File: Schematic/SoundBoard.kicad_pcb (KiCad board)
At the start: 4 copper layers, 50 x 50 mm, 50 parts, among them J1 USB_B_Micro, J2 Conn_ARM_JTAG_SWD_10, SW1 SW_Push, SW2 SW_Push, U1 AMS1117-3.3, U2 STM32F405RGTx, U3 MCP4021-xxxxSN, U4 LM4562, U5 W25Q128JVS, Y1 25Mhz

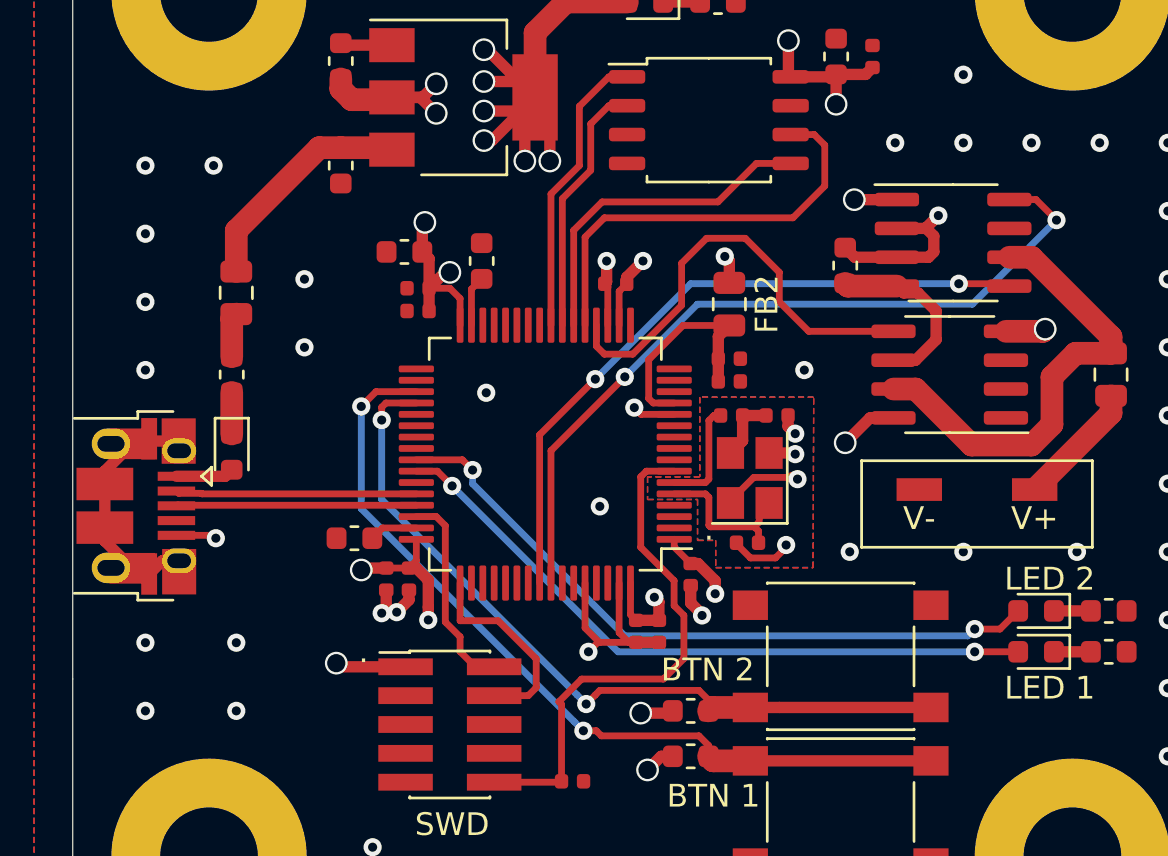
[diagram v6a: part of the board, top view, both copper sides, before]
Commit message: Modify manufacturing output per JLC
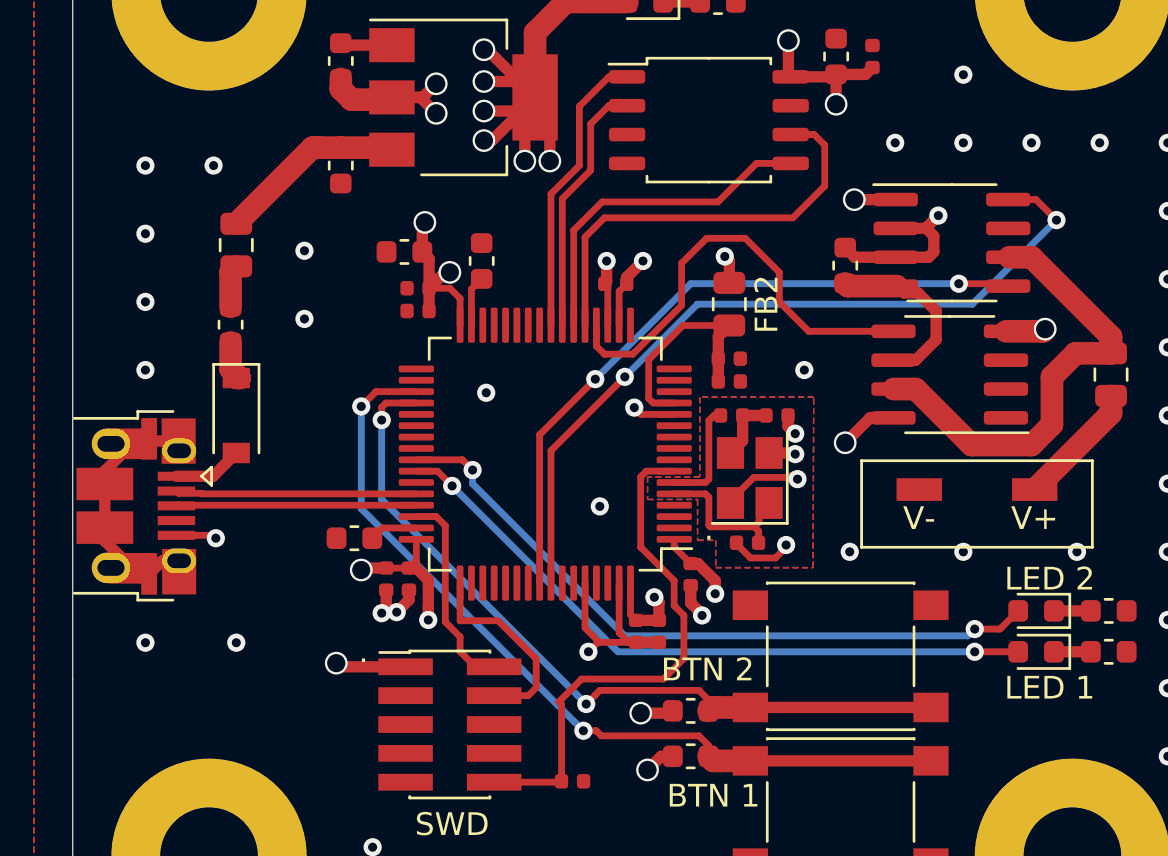
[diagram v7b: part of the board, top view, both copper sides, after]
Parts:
- D1: footprint Diode_SMD:D_0603_1608Metric -> Diode_SMD:D_SOD-123
- moved F1 2.20 mm to (66.8, 112.0)
- moved FB1 2.10 mm to (67.0, 108.5)
- moved D1 1.61 mm to (67.0, 116.0)
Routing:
- net Net-(C1-Pad1): track 10.2 -> 8.27 mm
- net VDD: track 2.55 -> 3.06 mm
- net GND: vias 65 -> 63
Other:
- board text added: "JLCJLCJLCJLC"
- board text removed: "JLCJLCJLC"
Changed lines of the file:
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@@
   )
   (setup
-    (last_trace_width 0.5)
+    (last_trace_width 1)
     (user_trace_width 0.3)
     (user_trace_width 0.4)
@@
     (add_net VDD)
   )
+  (module Diode_SMD:D_SOD-123 (layer F.Cu)
+    (at 67 116 270)
+    (descr SOD-123)
+    (tags SOD-123)
+    (attr smd)
+    (fp_text reference D1 (at 0 -2 90) (layer F.Fab)
+      (effects (font (size 1 1) (thickness 0.15)))
+    )
+    (fp_text value D_Schottky (at -0.25 -3 90) (layer F.Fab)
+      (effects (font (size 1 1) (thickness 0.15)))
+    )
+    (fp_line (start -2.25 -1) (end 1.65 -1) (layer F.SilkS) (width 0.12))
+    (fp_line (start -2.25 1) (end 1.65 1) (layer F.SilkS) (width 0.12))
+    (fp_line (start -2.35 -1.15) (end -2.35 1.15) (layer F.CrtYd) (width 0.05))
+    (fp_line (start 2.35 1.15) (end -2.35 1.15) (layer F.CrtYd) (width 0.05))
+    (fp_line (start 2.35 -1.15) (end 2.35 1.15) (layer F.CrtYd) (width 0.05))
+    (fp_line (start -2.35 -1.15) (end 2.35 -1.15) (layer F.CrtYd) (width 0.05))
+    (fp_line (start -1.4 -0.9) (end 1.4 -0.9) (layer F.Fab) (width 0.1))
+    (fp_line (start 1.4 -0.9) (end 1.4 0.9) (layer F.Fab) (width 0.1))
+    (fp_line (start 1.4 0.9) (end -1.4 0.9) (layer F.Fab) (width 0.1))
+    (fp_line (start -1.4 0.9) (end -1.4 -0.9) (layer F.Fab) (width 0.1))
+    (fp_line (start -0.75 0) (end -0.35 0) (layer F.Fab) (width 0.1))
+    (fp_line (start -0.35 0) (end -0.35 -0.55) (layer F.Fab) (width 0.1))
+    (fp_line (start -0.35 0) (end -0.35 0.55) (layer F.Fab) (width 0.1))
+    (fp_line (start -0.35 0) (end 0.25 -0.4) (layer F.Fab) (width 0.1))
+    (fp_line (start 0.25 -0.4) (end 0.25 0.4) (layer F.Fab) (width 0.1))
+    (fp_line (start 0.25 0.4) (end -0.35 0) (layer F.Fab) (width 0.1))
+    (fp_line (start 0.25 0) (end 0.75 0) (layer F.Fab) (width 0.1))
+    (fp_line (start -2.25 -1) (end -2.25 1) (layer F.SilkS) (width 0.12))
+    (fp_text user %R (at 0 -2 90) (layer F.Fab)
+      (effects (font (size 1 1) (thickness 0.15)))
+    )
+    (pad 2 smd rect (at 1.65 0 270) (size 0.9 1.2) (layers F.Cu F.Paste F.Mask)
+      (net 17 VDD))
+    (pad 1 smd rect (at -1.65 0 270) (size 0.9 1.2) (layers F.Cu F.Paste F.Mask)
+      (net 3 "Net-(D1-Pad1)"))
+    (model ${KISYS3DMOD}/Diode_SMD.3dshapes/D_SOD-123.wrl
+      (at (xyz 0 0 0))
+      (scale (xyz 1 1 1))
+      (rotate (xyz 0 0 0))
+    )
+  )
   (module Package_SO:SOIC-8_3.9x4.9mm_P1.27mm (layer F.Cu)
     (at 98.4 114.2 180)
@@
   )
   (module Inductor_SMD:L_0805_2012Metric (layer F.Cu)
-    (at 67 110.6 270)
+    (at 67 108.5 270)
     (descr "Inductor SMD 0805 (2012 Metric), square (rectangular) end terminal, IPC_7351 nominal, (Body size source: https://docs.google.com/spreadsheets/d/1BsfQQcO9C6DZCsRaXUlFlo91Tg2WpOkGARC1WS5S8t0/edit?usp=sharing), generated with kicad-footprint-generator")
     (tags inductor)
@@
     )
   )
-  (module Diode_SMD:D_0603_1608Metric (layer F.Cu)
-    (at 66.8 117.6 270)
-    (descr "Diode SMD 0603 (1608 Metric), square (rectangular) end terminal, IPC_7351 nominal, (Body size source: http://www.tortai-tech.com/upload/download/2011102023233369053.pdf), generated with kicad-footprint-generator")
-    (tags diode)
-    (attr smd)
-    (fp_text reference D1 (at 0 -1.43 90) (layer F.Fab)
-      (effects (font (size 1 1) (thickness 0.15)))
-    )
-    (fp_text value D_Schottky (at 0.2 -5 180) (layer F.Fab)
-      (effects (font (size 1 1) (thickness 0.15)))
-    )
-    (fp_line (start 0.8 -0.4) (end -0.5 -0.4) (layer F.Fab) (width 0.1))
-    (fp_line (start -0.5 -0.4) (end -0.8 -0.1) (layer F.Fab) (width 0.1))
-    (fp_line (start -0.8 -0.1) (end -0.8 0.4) (layer F.Fab) (width 0.1))
-    (fp_line (start -0.8 0.4) (end 0.8 0.4) (layer F.Fab) (width 0.1))
-    (fp_line (start 0.8 0.4) (end 0.8 -0.4) (layer F.Fab) (width 0.1))
-    (fp_line (start 0.8 -0.735) (end -1.485 -0.735) (layer F.SilkS) (width 0.12))
-    (fp_line (start -1.485 -0.735) (end -1.485 0.735) (layer F.SilkS) (width 0.12))
-    (fp_line (start -1.485 0.735) (end 0.8 0.735) (layer F.SilkS) (width 0.12))
-    (fp_line (start -1.48 0.73) (end -1.48 -0.73) (layer F.CrtYd) (width 0.05))
-    (fp_line (start -1.48 -0.73) (end 1.48 -0.73) (layer F.CrtYd) (width 0.05))
-    (fp_line (start 1.48 -0.73) (end 1.48 0.73) (layer F.CrtYd) (width 0.05))
-    (fp_line (start 1.48 0.73) (end -1.48 0.73) (layer F.CrtYd) (width 0.05))
-    (fp_text user %R (at 0 0 90) (layer F.Fab)
-      (effects (font (size 0.4 0.4) (thickness 0.06)))
-    )
-    (pad 1 smd roundrect (at -0.7875 0 270) (size 0.875 0.95) (layers F.Cu F.Paste F.Mask) (roundrect_rratio 0.25)
-      (net 3 "Net-(D1-Pad1)"))
-    (pad 2 smd roundrect (at 0.7875 0 270) (size 0.875 0.95) (layers F.Cu F.Paste F.Mask) (roundrect_rratio 0.25)
-      (net 17 VDD))
-    (model ${KISYS3DMOD}/Diode_SMD.3dshapes/D_0603_1608Metric.wrl
-      (at (xyz 0 0 0))
-      (scale (xyz 1 1 1))
-      (rotate (xyz 0 0 0))
-    )
-  )
   (module LED_SMD:LED_0603_1608Metric (layer F.Cu)
     (at 85 97.8 180)
@@
   )
   (module Fuse:Fuse_0603_1608Metric (layer F.Cu)
-    (at 66.8 114.2 270)
+    (at 66.75 112 270)
     (descr "Fuse SMD 0603 (1608 Metric), square (rectangular) end terminal, IPC_7351 nominal, (Body size source: http://www.tortai-tech.com/upload/download/2011102023233369053.pdf), generated with kicad-footprint-generator")
     (tags resistor)
@@
   )
   (module Package_SO:SOIC-8_3.9x4.9mm_P1.27mm (layer F.Cu)
-    (at 98.55 108.4)
+    (at 98.5 108.4)
     (descr "SOIC, 8 Pin (JEDEC MS-012AA, https://www.analog.com/media/en/package-pcb-resources/package/pkg_pdf/soic_narrow-r/r_8.pdf), generated with kicad-footprint-generator ipc_gullwing_generator.py")
     (tags "SOIC SO")
@@
     (effects (font (size 1 1) (thickness 0.15)) (justify mirror))
   )
-  (gr_text JLCJLCJLC (at 65.4 128.8) (layer B.SilkS)
+  (gr_text "JLCJLCJLCJLC\n" (at 68.5 129.25) (layer B.SilkS)
     (effects (font (size 1 1) (thickness 0.15)) (justify mirror))
   )
@@
   (via (at 74.061026 124.655978) (size 0.8) (drill 0.4) (layers F.Cu B.Cu) (net 1))
   (segment (start 74.6 124.117004) (end 74.061026 124.655978) (width 0.5) (layer F.Cu) (net 1))
-  (via (at 70 110) (size 0.8) (drill 0.4) (layers F.Cu B.Cu) (net 1))
-  (via (at 70 113) (size 0.8) (drill 0.4) (layers F.Cu B.Cu) (net 1))
+  (via (at 70 108.75) (size 0.8) (drill 0.4) (layers F.Cu B.Cu) (net 1))
+  (via (at 70 111.75) (size 0.8) (drill 0.4) (layers F.Cu B.Cu) (net 1))
   (via (at 78 115) (size 0.8) (drill 0.4) (layers F.Cu B.Cu) (net 1))
   (via (at 63 105) (size 0.8) (drill 0.4) (layers F.Cu B.Cu) (net 1))
@@
   (via (at 63 111) (size 0.8) (drill 0.4) (layers F.Cu B.Cu) (net 1))
   (via (at 63 126) (size 0.8) (drill 0.4) (layers F.Cu B.Cu) (net 1))
-  (via (at 63 129) (size 0.8) (drill 0.4) (layers F.Cu B.Cu) (net 1))
-  (via (at 67 129) (size 0.8) (drill 0.4) (layers F.Cu B.Cu) (net 1))
   (via (at 67 126) (size 0.8) (drill 0.4) (layers F.Cu B.Cu) (net 1))
   (via (at 73 135) (size 0.8) (drill 0.4) (layers F.Cu B.Cu) (net 1))
@@
   (segment (start 105.5 115.9) (end 105.5 115.1375) (width 1) (layer F.Cu) (net 2))
   (segment (start 102.14 119.26) (end 105.5 115.9) (width 1) (layer F.Cu) (net 2))
-  (segment (start 66.8 116.8125) (end 66.8 114.9875) (width 1) (layer F.Cu) (net 3))
+  (segment (start 67 114.35) (end 67.15 114.35) (width 1) (layer F.Cu) (net 3))
+  (segment (start 66.75 113.95) (end 66.75 112.7875) (width 1) (layer F.Cu) (net 3))
+  (segment (start 67.15 114.35) (end 66.75 113.95) (width 1) (layer F.Cu) (net 3))
   (segment (start 87.4125 97.8) (end 85.7875 97.8) (width 0.5) (layer F.Cu) (net 4))
   (segment (start 102.9875 126.4) (end 104.6125 126.4) (width 0.5) (layer F.Cu) (net 5))
@@
   (segment (start 73.7625 104.2125) (end 73.85 104.3) (width 1) (layer F.Cu) (net 9))
   (segment (start 71.6 104.2125) (end 73.7625 104.2125) (width 1) (layer F.Cu) (net 9))
-  (segment (start 67 107.8625) (end 70.65 104.2125) (width 1) (layer F.Cu) (net 9))
-  (segment (start 67 109.6625) (end 67 107.8625) (width 1) (layer F.Cu) (net 9))
+  (segment (start 70.35 104.2125) (end 70.65 104.2125) (width 1) (layer F.Cu) (net 9))
+  (segment (start 67 107.5625) (end 70.35 104.2125) (width 1) (layer F.Cu) (net 9))
   (segment (start 90.085 120.215) (end 90.45 119.85) (width 0.3) (layer F.Cu) (net 10))
   (segment (start 87.799999 119.599999) (end 87.799999 120.830001) (width 0.3) (layer F.Cu) (net 10))
@@
   (segment (start 102 109.035) (end 105.5 112.535) (width 1) (layer F.Cu) (net 16))
   (segment (start 101.025 109.035) (end 102 109.035) (width 1) (layer F.Cu) (net 16))
-  (segment (start 66.5125 118.675) (end 66.8 118.3875) (width 0.5) (layer F.Cu) (net 17))
-  (segment (start 64.365 118.675) (end 66.5125 118.675) (width 0.5) (layer F.Cu) (net 17))
+  (segment (start 65.975 118.675) (end 67 117.65) (width 0.5) (layer F.Cu) (net 17))
+  (segment (start 64.365 118.675) (end 65.975 118.675) (width 0.5) (layer F.Cu) (net 17))
   (via (at 76.5 119.1) (size 0.8) (drill 0.4) (layers F.Cu B.Cu) (net 18))
   (segment (start 74.925 118.45) (end 75.85 118.45) (width 0.3) (layer F.Cu) (net 18))
@@
   (segment (start 77.4 118.4) (end 77.4 119) (width 0.3) (layer B.Cu) (net 19))
   (segment (start 77.4 119) (end 84.1 125.7) (width 0.3) (layer B.Cu) (net 19))
-  (segment (start 66.8 111.7375) (end 67 111.5375) (width 1) (layer F.Cu) (net 20))
-  (segment (start 66.8 113.4125) (end 66.8 111.7375) (width 1) (layer F.Cu) (net 20))
+  (segment (start 66.75 109.6875) (end 67 109.4375) (width 1) (layer F.Cu) (net 20))
+  (segment (start 66.75 111.2125) (end 66.75 109.6875) (width 1) (layer F.Cu) (net 20))
   (segment (start 76.85 125.739996) (end 76.200032 125.090028) (width 0.3) (layer F.Cu) (net 21))
   (segment (start 77.52 127.06) (end 76.85 126.39) (width 0.3) (layer F.Cu) (net 21))
